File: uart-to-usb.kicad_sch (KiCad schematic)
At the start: 0 parts

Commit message: Setup basic schematic
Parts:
- added C1, C3: 100nF, symbol Device:C
- added C2: 4.7uF, symbol Device:C
- added C4: 10nF, symbol Device:C
- added FB1: FerriteBead, symbol Device:FerriteBead
- added J1: USB_C_Receptacle_USB2.0_16P, symbol Connector:USB_C_Receptacle_USB2.0_16P
- added J2: Conn_01x02_Pin, symbol Connector:Conn_01x02_Pin
- added R1, R2: 5.1k, symbol Device:R
- added U1: FT232RL, Package_SO:SSOP-28_5.3x10.2mm_P0.65mm, symbol Interface_USB:FT232RL
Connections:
- new net: C4.1, FB1.2, J1.A4 (VBUS), J1.A9 (VBUS), J1.B4 (VBUS), J1.B9 (VBUS)
- new net: J1.A5 (CC1), R2.1
- new net: J1.B5 (CC2), R1.1
- new net: C1.1, U1.17 (3V3OUT)
- new net: J2.2 (Pin_2), U1.1 (TXD)
- new net: J2.1 (Pin_1), U1.5 (RXD)
- new net +5V: C2.1, C3.1, FB1.1, U1.20 (VCC), U1.4 (VCCIO)
- new net D+: J1.A6 (D+), J1.B6 (D+), U1.15 (USBD+)
- new net D-: J1.A7 (D-), J1.B7 (D-), U1.16 (USBD-)
- new net GND: C1.2, C2.2, C3.2, C4.2, J1.A1 (GND), J1.A12 (GND), J1.B1 (GND), J1.B12 (GND), R1.2, R2.2, U1.18 (GND), U1.21 (GND), U1.25 (AGND), U1.26 (TEST), U1.7 (GND)
- new net SBU1: J1.A8 (SBU1)
- new net SBU2: J1.B8 (SBU2)

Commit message: Assign footprints
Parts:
- C1, C3, C4: footprint (none) -> Capacitor_SMD:C_0805_2012Metric
- C2: footprint (none) -> Capacitor_SMD:C_1206_3216Metric
- J1: footprint (none) -> Connector_USB:USB_C_Receptacle_GCT_USB4105-xx-A_16P_TopMnt_Horizontal
- R1, R2: footprint (none) -> Resistor_SMD:R_0805_2012Metric
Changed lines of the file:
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@@
 			)
 		)
-		(property "Footprint" ""
+		(property "Footprint" "Capacitor_SMD:C_1206_3216Metric"
 			(at 119.0752 44.45 0)
 			(hide yes)
@@
 			)
 		)
-		(property "Footprint" ""
+		(property "Footprint" "Connector_USB:USB_C_Receptacle_GCT_USB4105-xx-A_16P_TopMnt_Horizontal"
 			(at 55.88 90.17 0)
 			(hide yes)
@@
 			)
 		)
-		(property "Footprint" ""
+		(property "Footprint" "Capacitor_SMD:C_0805_2012Metric"
 			(at 112.7252 74.93 0)
 			(hide yes)
@@
 			)
 		)
-		(property "Footprint" ""
+		(property "Footprint" "Resistor_SMD:R_0805_2012Metric"
 			(at 79.502 91.44 90)
 			(hide yes)
@@
 			)
 		)
-		(property "Footprint" ""
+		(property "Footprint" "Resistor_SMD:R_0805_2012Metric"
 			(at 90.932 91.44 90)
 			(hide yes)
@@
 			)
 		)
-		(property "Footprint" ""
+		(property "Footprint" "Capacitor_SMD:C_0805_2012Metric"
 			(at 82.2452 69.85 0)
 			(hide yes)
@@
 			)
 		)
-		(property "Footprint" ""
+		(property "Footprint" "Capacitor_SMD:C_0805_2012Metric"
 			(at 108.9152 44.45 0)
 			(hide yes)

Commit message: Start layout
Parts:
- FB1: footprint (none) -> Inductor_SMD:L_0805_2012Metric
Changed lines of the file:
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@@
 			)
 		)
-		(property "Footprint" ""
+		(property "Footprint" "Inductor_SMD:L_0805_2012Metric"
 			(at 70.612 53.34 90)
 			(hide yes)

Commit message: Initial PCB route
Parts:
- added J3: Conn_01x02_Pin, Connector_PinSocket_2.00mm:PinSocket_1x02_P2.00mm_Horizontal, symbol Connector:Conn_01x02_Pin
- J2: footprint (none) -> Connector_JST:JST_GH_SM02B-GHS-TB_1x02-1MP_P1.25mm_Horizontal
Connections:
- net at J2.2 (Pin_2), U1.1 (TXD): now also J3.2 (Pin_2)
- net at J2.1 (Pin_1), U1.5 (RXD): now also J3.1 (Pin_1)
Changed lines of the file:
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@@
 	(paper "A4")
+	(junction
+		(at 196.85 77.47)
+		(diameter 0)
+		(color 0 0 0 0)
+	)
 	(junction
 		(at 143.51 63.5)
@@
 	)
 	(junction
+		(at 194.31 80.01)
+		(diameter 0)
+		(color 0 0 0 0)
+	)
+	(junction
 		(at 146.05 127)
 		(diameter 0)
@@
 	(wire
 		(pts
+			(xy 194.31 88.9) (xy 203.2 88.9)
+		)
+		(stroke
+			(width 0)
+			(type default)
+		)
+	)
+	(wire
+		(pts
 			(xy 107.95 36.83) (xy 113.03 36.83)
 		)
@@
 	(wire
 		(pts
+			(xy 194.31 80.01) (xy 194.31 88.9)
+		)
+		(stroke
+			(width 0)
+			(type default)
+		)
+	)
+	(wire
+		(pts
+			(xy 196.85 77.47) (xy 196.85 86.36)
+		)
+		(stroke
+			(width 0)
+			(type default)
+		)
+	)
+	(wire
+		(pts
 			(xy 67.31 80.01) (xy 92.71 80.01)
 		)
@@
 	(wire
 		(pts
-			(xy 163.83 80.01) (xy 203.2 80.01)
+			(xy 163.83 80.01) (xy 194.31 80.01)
 		)
 		(stroke
@@
 	(wire
 		(pts
-			(xy 163.83 77.47) (xy 203.2 77.47)
+			(xy 196.85 86.36) (xy 203.2 86.36)
+		)
+		(stroke
+			(width 0)
+			(type default)
+		)
+	)
+	(wire
+		(pts
+			(xy 196.85 77.47) (xy 203.2 77.47)
+		)
+		(stroke
+			(width 0)
+			(type default)
+		)
+	)
+	(wire
+		(pts
+			(xy 163.83 77.47) (xy 196.85 77.47)
 		)
 		(stroke
@@
 		(pts
 			(xy 81.28 82.55) (xy 81.28 87.63)
+		)
+		(stroke
+			(width 0)
+			(type default)
+		)
+	)
+	(wire
+		(pts
+			(xy 194.31 80.01) (xy 203.2 80.01)
 		)
 		(stroke
@@
 	)
 	(symbol
+		(lib_id "Connector:Conn_01x02_Pin")
+		(at 208.28 88.9 180)
+		(unit 1)
+		(body_style 1)
+		(exclude_from_sim no)
+		(in_bom yes)
+		(on_board yes)
+		(in_pos_files yes)
+		(dnp no)
+		(fields_autoplaced yes)
+		(property "Reference" "J3"
+			(at 209.55 86.3599 0)
+			(show_name no)
+			(do_not_autoplace no)
+			(effects
+				(font
+					(size 1.27 1.27)
+				)
+				(justify right)
+			)
+		)
+		(property "Value" "Conn_01x02_Pin"
+			(at 209.55 88.8999 0)
+			(show_name no)
+			(do_not_autoplace no)
+			(effects
+				(font
+					(size 1.27 1.27)
+				)
+				(justify right)
+			)
+		)
+		(property "Footprint" "Connector_PinSocket_2.00mm:PinSocket_1x02_P2.00mm_Horizontal"
+			(at 208.28 88.9 0)
+			(hide yes)
+			(show_name no)
+			(do_not_autoplace no)
+			(effects
+				(font
+					(size 1.27 1.27)
+				)
+			)
+		)
+		(property "Datasheet" ""
+			(at 208.28 88.9 0)
+			(hide yes)
+			(show_name no)
+			(do_not_autoplace no)
+			(effects
+				(font
+					(size 1.27 1.27)
+				)
+			)
+		)
+		(property "Description" "Generic connector, single row, 01x02, script generated"
+			(at 208.28 88.9 0)
+			(hide yes)
+			(show_name no)
+			(do_not_autoplace no)
+			(effects
+				(font
+					(size 1.27 1.27)
+				)
+			)
+		)
+		(pin "1"
+		)
+		(pin "2"
+		)
+		(instances
+			(project "uart-to-usb"
+				(path "/bba0d1c0-0815-4255-9c21-1ba5a01ec5bc"
+					(reference "J3")
+					(unit 1)
+				)
+			)
+		)
+	)
+	(symbol
 		(lib_id "power:GND")
 		(at 81.28 69.85 0)
@@
 			)
 		)
-		(property "Footprint" ""
+		(property "Footprint" "Connector_JST:JST_GH_SM02B-GHS-TB_1x02-1MP_P1.25mm_Horizontal"
 			(at 208.28 80.01 0)
 			(hide yes)

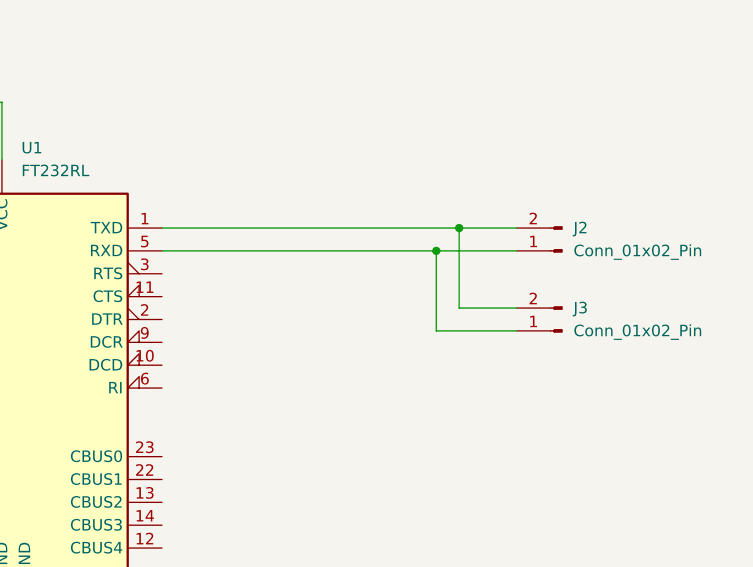
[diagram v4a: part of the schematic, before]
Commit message: Use single input connector
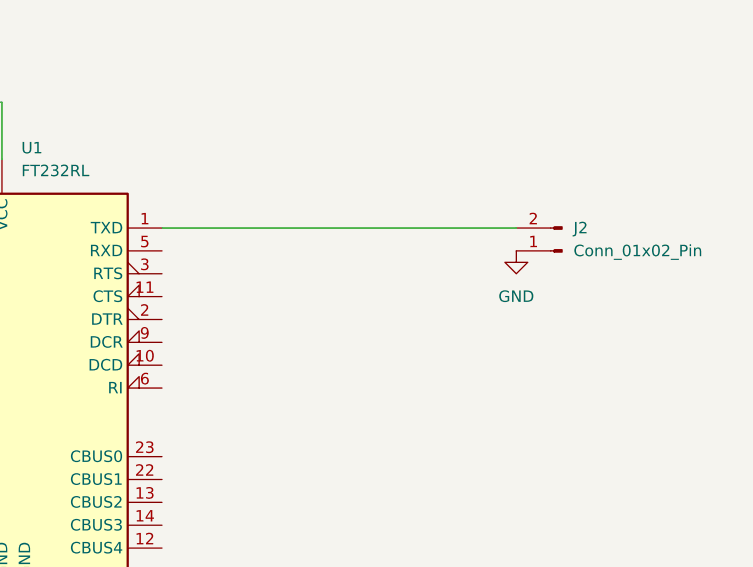
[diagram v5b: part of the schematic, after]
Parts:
- removed J3: Conn_01x02_Pin, Connector_PinSocket_2.00mm:PinSocket_1x02_P2.00mm_Horizontal, symbol Connector:Conn_01x02_Pin
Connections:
- net GND: now also J2.1 (Pin_1)
- net at U1.5 (RXD): no longer J2.1 (Pin_1)
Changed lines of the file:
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@@
 	(paper "A4")
-	(junction
-		(at 196.85 77.47)
-		(diameter 0)
-		(color 0 0 0 0)
-	)
 	(junction
 		(at 143.51 63.5)
@@
 	)
 	(junction
-		(at 194.31 80.01)
-		(diameter 0)
-		(color 0 0 0 0)
-	)
-	(junction
 		(at 146.05 127)
 		(diameter 0)
@@
 	(wire
 		(pts
-			(xy 194.31 88.9) (xy 203.2 88.9)
-		)
-		(stroke
-			(width 0)
-			(type default)
-		)
-	)
-	(wire
-		(pts
 			(xy 107.95 36.83) (xy 113.03 36.83)
 		)
@@
 	(wire
 		(pts
-			(xy 194.31 80.01) (xy 194.31 88.9)
-		)
-		(stroke
-			(width 0)
-			(type default)
-		)
-	)
-	(wire
-		(pts
-			(xy 196.85 77.47) (xy 196.85 86.36)
-		)
-		(stroke
-			(width 0)
-			(type default)
-		)
-	)
-	(wire
-		(pts
 			(xy 67.31 80.01) (xy 92.71 80.01)
 		)
@@
 	(wire
 		(pts
-			(xy 163.83 80.01) (xy 194.31 80.01)
-		)
-		(stroke
-			(width 0)
-			(type default)
-		)
-	)
-	(wire
-		(pts
 			(xy 113.03 36.83) (xy 118.11 36.83)
 		)
@@
 	(wire
 		(pts
-			(xy 196.85 86.36) (xy 203.2 86.36)
-		)
-		(stroke
-			(width 0)
-			(type default)
-		)
-	)
-	(wire
-		(pts
-			(xy 196.85 77.47) (xy 203.2 77.47)
-		)
-		(stroke
-			(width 0)
-			(type default)
-		)
-	)
-	(wire
-		(pts
-			(xy 163.83 77.47) (xy 196.85 77.47)
+			(xy 163.83 77.47) (xy 203.2 77.47)
 		)
 		(stroke
@@
 		(pts
 			(xy 81.28 82.55) (xy 81.28 87.63)
-		)
-		(stroke
-			(width 0)
-			(type default)
-		)
-	)
-	(wire
-		(pts
-			(xy 194.31 80.01) (xy 203.2 80.01)
 		)
 		(stroke
@@
 	)
 	(symbol
-		(lib_id "Connector:Conn_01x02_Pin")
-		(at 208.28 88.9 180)
-		(unit 1)
-		(body_style 1)
-		(exclude_from_sim no)
-		(in_bom yes)
-		(on_board yes)
-		(in_pos_files yes)
-		(dnp no)
-		(fields_autoplaced yes)
-		(property "Reference" "J3"
-			(at 209.55 86.3599 0)
-			(show_name no)
-			(do_not_autoplace no)
-			(effects
-				(font
-					(size 1.27 1.27)
-				)
-				(justify right)
-			)
-		)
-		(property "Value" "Conn_01x02_Pin"
-			(at 209.55 88.8999 0)
-			(show_name no)
-			(do_not_autoplace no)
-			(effects
-				(font
-					(size 1.27 1.27)
-				)
-				(justify right)
-			)
-		)
-		(property "Footprint" "Connector_PinSocket_2.00mm:PinSocket_1x02_P2.00mm_Horizontal"
-			(at 208.28 88.9 0)
-			(hide yes)
-			(show_name no)
-			(do_not_autoplace no)
-			(effects
-				(font
-					(size 1.27 1.27)
-				)
-			)
-		)
-		(property "Datasheet" ""
-			(at 208.28 88.9 0)
-			(hide yes)
-			(show_name no)
-			(do_not_autoplace no)
-			(effects
-				(font
-					(size 1.27 1.27)
-				)
-			)
-		)
-		(property "Description" "Generic connector, single row, 01x02, script generated"
-			(at 208.28 88.9 0)
-			(hide yes)
-			(show_name no)
-			(do_not_autoplace no)
-			(effects
-				(font
-					(size 1.27 1.27)
-				)
-			)
-		)
-		(pin "1"
-		)
-		(pin "2"
-		)
-		(instances
-			(project "uart-to-usb"
-				(path "/bba0d1c0-0815-4255-9c21-1ba5a01ec5bc"
-					(reference "J3")
-					(unit 1)
-				)
-			)
-		)
-	)
-	(symbol
 		(lib_id "power:GND")
 		(at 81.28 69.85 0)
@@
 					(unit 1)
 				)
+			)
+		)
+	)
+	(symbol
+		(lib_id "power:GND")
+		(at 203.2 80.01 0)
+		(unit 1)
+		(body_style 1)
+		(exclude_from_sim no)
+		(in_bom yes)
+		(on_board yes)
+		(in_pos_files yes)
+		(dnp no)
+		(fields_autoplaced yes)
+		(property "Reference" "#PWR011"
+			(at 203.2 86.36 0)
+			(hide yes)
+			(show_name no)
+			(do_not_autoplace no)
+			(effects
+				(font
+					(size 1.27 1.27)
+				)
+			)
+		)
+		(property "Value" "GND"
+			(at 203.2 85.09 0)
+			(show_name no)
+			(do_not_autoplace no)
+			(effects
+				(font
+					(size 1.27 1.27)
+				)
+			)
+		)
+		(property "Footprint" ""
+			(at 203.2 80.01 0)
+			(hide yes)
+			(show_name no)
+			(do_not_autoplace no)
+			(effects
+				(font
+					(size 1.27 1.27)
+				)
+			)
+		)
+		(property "Datasheet" ""
+			(at 203.2 80.01 0)
+			(hide yes)
+			(show_name no)
+			(do_not_autoplace no)
+			(effects
+				(font
+					(size 1.27 1.27)
+				)
+			)
+		)
+		(property "Description" "Power symbol creates a global label with name \"GND\" , ground"
+			(at 203.2 80.01 0)
+			(hide yes)
+			(show_name no)
+			(do_not_autoplace no)
+			(effects
+				(font
+					(size 1.27 1.27)
+				)
+			)
+		)
+		(pin "1"
+		)
+		(instances
+			(project "uart-to-usb"
+				(path "/bba0d1c0-0815-4255-9c21-1ba5a01ec5bc"
+					(reference "#PWR011")
+					(unit 1)
+				)

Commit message: Add part for BOM
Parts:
- C1, C3: LSCS (none) -> C1711
- C2: LSCS (none) -> C1746
- C4: LSCS (none) -> C1710
- FB1: LSCS (none) -> C1009
- J1: LSCS (none) -> C3020560
- J2: LSCS (none) -> C189893
- R1, R2: footprint Resistor_SMD:R_0805_2012Metric -> Resistor_SMD:R_0603_1608Metric; LSCS (none) -> C23186
- U1: LSCS (none) -> C8690
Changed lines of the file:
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@@
+			)
+		)
+		(property "LSCS" "C1746"
+			(at 118.11 40.64 0)
+			(hide yes)
+			(show_name no)
+			(do_not_autoplace no)
+			(effects
+				(font
+					(size 1.27 1.27)
+				)
 			)
 		)
@@
 			)
 		)
+		(property "LSCS" "C3020560"
+			(at 52.07 90.17 0)
+			(hide yes)
+			(show_name no)
+			(do_not_autoplace no)
+			(effects
+				(font
+					(size 1.27 1.27)
+				)
+			)
+		)
 		(pin "A4"
 		)
@@
 			)
 		)
+		(property "LSCS" "C1711"
+			(at 111.76 71.12 0)
+			(hide yes)
+			(show_name no)
+			(do_not_autoplace no)
+			(effects
+				(font
+					(size 1.27 1.27)
+				)
+			)
+		)
 		(pin "2"
 		)
@@
 			)
 		)
-		(property "Footprint" "Resistor_SMD:R_0805_2012Metric"
+		(property "Footprint" "Resistor_SMD:R_0603_1608Metric"
 			(at 79.502 91.44 90)
 			(hide yes)
@@
 		)
 		(property "Description" "Resistor"
+			(at 81.28 91.44 0)
+			(hide yes)
+			(show_name no)
+			(do_not_autoplace no)
+			(effects
+				(font
+					(size 1.27 1.27)
+				)
+			)
+		)
+		(property "LSCS" "C23186"
 			(at 81.28 91.44 0)
 			(hide yes)
@@
 			)
 		)
-		(property "Footprint" "Resistor_SMD:R_0805_2012Metric"
+		(property "Footprint" "Resistor_SMD:R_0603_1608Metric"
 			(at 90.932 91.44 90)
 			(hide yes)
@@
 		)
 		(property "Description" "Resistor"
+			(at 92.71 91.44 0)
+			(hide yes)
+			(show_name no)
+			(do_not_autoplace no)
+			(effects
+				(font
+					(size 1.27 1.27)
+				)
+			)
+		)
+		(property "LSCS" "C23186"
 			(at 92.71 91.44 0)
 			(hide yes)
@@
 			)
 		)
+		(property "LSCS" "C1710"
+			(at 81.28 66.04 0)
+			(hide yes)
+			(show_name no)
+			(do_not_autoplace no)
+			(effects
+				(font
+					(size 1.27 1.27)
+				)
+			)
+		)
 		(pin "1"
 		)
@@
 		)
 		(property "Description" "Unpolarized capacitor"
+			(at 107.95 40.64 0)
+			(hide yes)
+			(show_name no)
+			(do_not_autoplace no)
+			(effects
+				(font
+					(size 1.27 1.27)
+				)
+			)
+		)
+		(property "LSCS" "C1711"
 			(at 107.95 40.64 0)
 			(hide yes)
@@
 			)
 		)
+		(property "LSCS" "C8690"
+			(at 143.51 95.25 0)
+			(hide yes)
+			(show_name no)
+			(do_not_autoplace no)
+			(effects
+				(font
+					(size 1.27 1.27)
+				)
+			)
+		)
 		(pin "2"
 		)
@@
 			)
 		)
+		(property "LSCS" "C1009"
+			(at 72.39 53.34 0)
+			(hide yes)
+			(show_name no)
+			(do_not_autoplace no)
+			(effects
+				(font
+					(size 1.27 1.27)
+				)
+			)
+		)
 		(pin "2"
 		)
@@
 			(at 208.28 80.01 0)
 			(hide yes)
+			(show_name no)
+			(do_not_autoplace no)
+			(effects
+				(font
+					(size 1.27 1.27)
+				)
+			)
+		)
+		(property "LSCS" "C189893"
+			(at 208.28 80.01 0)
+			(hide yes)

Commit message: Fix usb-c alignment
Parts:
- C1, C3: LCSC (none) -> C1711; LSCS C1711 -> (none)
- C2: LCSC (none) -> C17936; LSCS C1746 -> (none)
- C4: LCSC (none) -> C1710; LSCS C1710 -> (none)
- FB1: LCSC (none) -> C1011; LSCS C1009 -> (none)
- J1: LCSC (none) -> C3020560; LSCS C3020560 -> (none)
- J2: LCSC (none) -> C189893; LSCS C189893 -> (none)
- R1, R2: LCSC (none) -> C23186; LSCS C23186 -> (none)
- U1: LCSC (none) -> C8690; LSCS C8690 -> (none)
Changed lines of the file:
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@@
 			)
 		)
-		(property "LSCS" "C1746"
+		(property "LCSC" "C17936"
 			(at 118.11 40.64 0)
 			(hide yes)
@@
 			)
 		)
-		(property "LSCS" "C3020560"
+		(property "LCSC" "C3020560"
 			(at 52.07 90.17 0)
 			(hide yes)
@@
 			)
 		)
-		(property "LSCS" "C1711"
+		(property "LCSC" "C1711"
 			(at 111.76 71.12 0)
 			(hide yes)
@@
 			)
 		)
-		(property "LSCS" "C23186"
+		(property "LCSC" "C23186"
 			(at 81.28 91.44 0)
 			(hide yes)
@@
 			)
 		)
-		(property "LSCS" "C23186"
+		(property "LCSC" "C23186"
 			(at 92.71 91.44 0)
 			(hide yes)
@@
 			)
 		)
-		(property "LSCS" "C1710"
+		(property "LCSC" "C1710"
 			(at 81.28 66.04 0)
 			(hide yes)
@@
 			)
 		)
-		(property "LSCS" "C1711"
+		(property "LCSC" "C1711"
 			(at 107.95 40.64 0)
 			(hide yes)
@@
 			)
 		)
-		(property "LSCS" "C8690"
+		(property "LCSC" "C8690"
 			(at 143.51 95.25 0)
 			(hide yes)
@@
 			)
 		)
-		(property "LSCS" "C1009"
+		(property "LCSC" "C1011"
 			(at 72.39 53.34 0)
 			(hide yes)
@@
 			)
 		)
-		(property "LSCS" "C189893"
+		(property "LCSC" "C189893"
 			(at 208.28 80.01 0)
 			(hide yes)
